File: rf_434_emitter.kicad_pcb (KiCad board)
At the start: 2 copper layers, 133 x 100 mm, 67 parts, among them J1 Conn_Coaxial, J2 Jack-DC, SW1 SW_DIP_x06, SW5 SW_SPDT, SW7 SW_SPDT, SW8 SW_SPDT, U1 HT12E, U2 TLP-434, U3 LM7805_TO220, X1 ENCODER_ANO

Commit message: DIP switch THT
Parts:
- SW2: renamed from SW1; footprint Button_Switch_SMD:SW_DIP_SPSTx06_Slide_6.7x16.8mm_W8.61mm_P2.54mm_LowProfile -> Button_Switch_THT:SW_DIP_SPSTx06_Slide_9.78x17.42mm_W7.62mm_P2.54mm
- moved SW2 7.81 mm to (174.0, 109.3)
- renumbered C4 to C1, C3 to C2, C5 to C3, C6 to C4, C1 to C5, C2 to C6, D14 to D1, D7 to D10, D8 to D11, D9 to D12, D10 to D13, D11 to D14, D12 to D15, D15 to D2, D13 to D3, D1 to D4, D2 to D5, D3 to D6, D4 to D7, D5 to D8, D6 to D9, H4 to H3, H3 to H4, JP5 to JP1, JP6 to JP2, JP1 to JP4, JP4 to JP5, JP2 to JP6, R29 to R1, R21 to R10, R22 to R11, R23 to R12, R24 to R13, R25 to R14, R26 to R15, R5 to R16, R3 to R17, R2 to R18, R1 to R19, R28 to R2, R4 to R20, R14 to R21, R13 to R22, R12 to R23, R11 to R24, R10 to R25, R9 to R26, R27 to R3, R15 to R4, R16 to R5, R17 to R6, R18 to R7, R19 to R8, R20 to R9, SW5 to SW1, SW7 to SW3, SW8 to SW4, U2 to U1, U3 to U2, U1 to U3
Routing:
- net GND: track 14.0 -> 16.2 mm

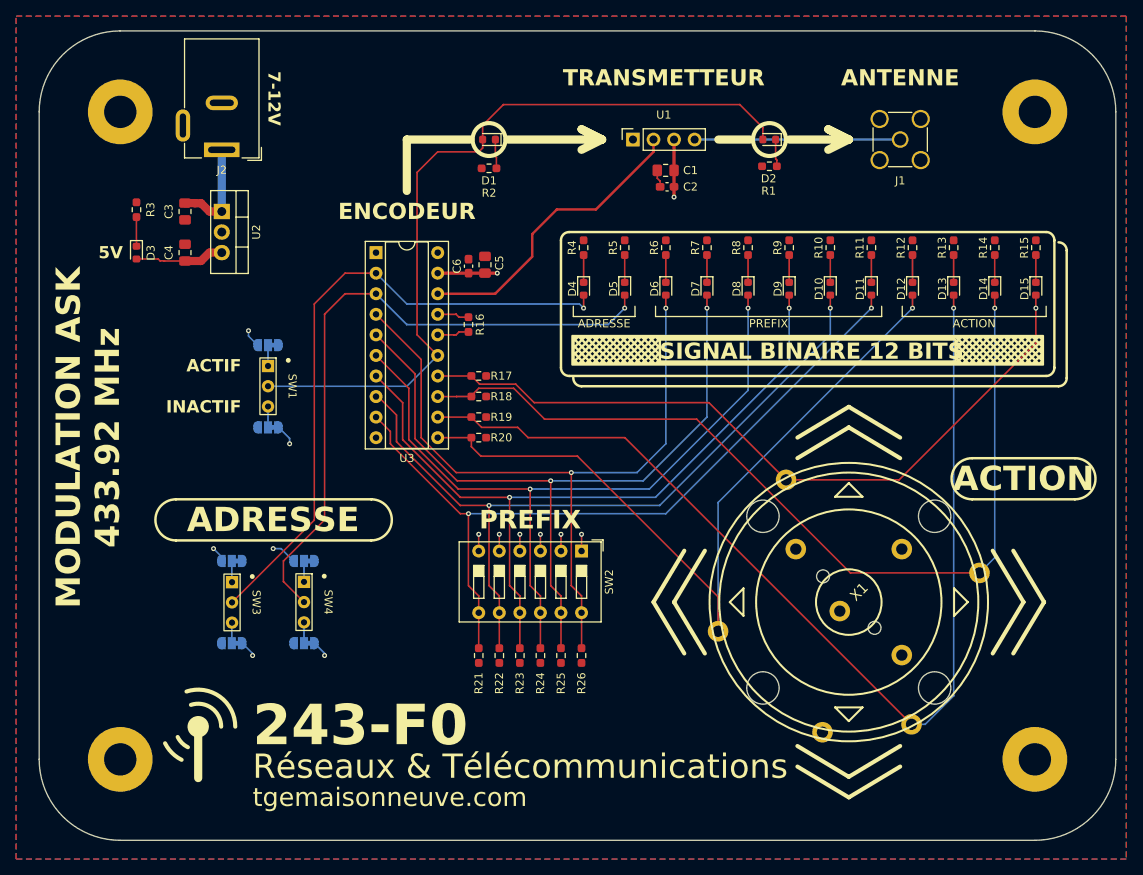
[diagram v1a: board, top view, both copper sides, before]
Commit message: Add D0-D3 connector
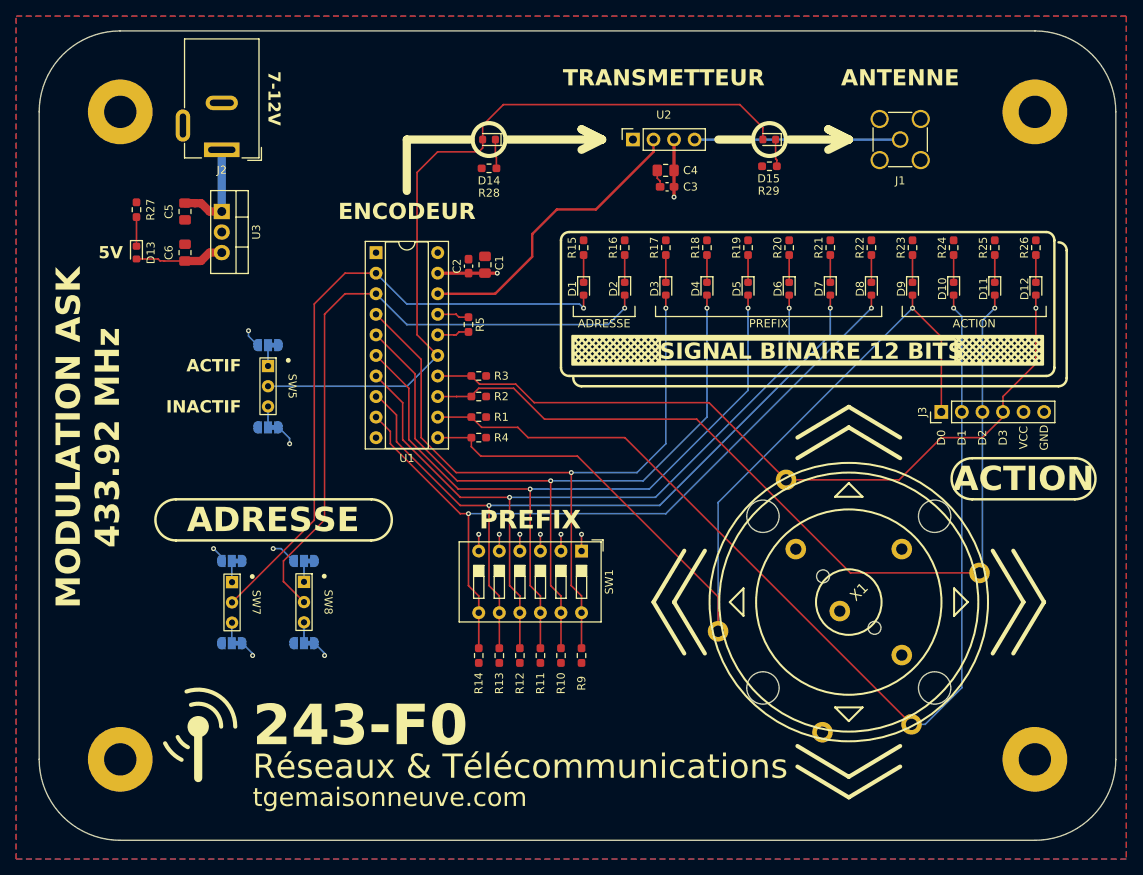
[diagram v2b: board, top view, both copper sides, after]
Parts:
- added J3: Conn_01x06, Connector_PinHeader_2.54mm:PinHeader_1x06_P2.54mm_Vertical, F.Cu at (218.4, 92.1)
- renumbered C5 to C1, C6 to C2, C2 to C3, C1 to C4, C3 to C5, C4 to C6, D4 to D1, D13 to D10, D14 to D11, D15 to D12, D3 to D13, D1 to D14, D2 to D15, D5 to D2, D6 to D3, D7 to D4, D8 to D5, D9 to D6, D10 to D7, D11 to D8, D12 to D9, H4 to H3, H3 to H4, JP4 to JP1, JP6 to JP2, JP5 to JP4, JP1 to JP5, JP2 to JP6, R19 to R1, R25 to R10, R24 to R11, R23 to R12, R22 to R13, R21 to R14, R4 to R15, R5 to R16, R6 to R17, R7 to R18, R8 to R19, R18 to R2, R9 to R20, R10 to R21, R11 to R22, R12 to R23, R13 to R24, R14 to R25, R15 to R26, R3 to R27, R2 to R28, R1 to R29, R17 to R3, R20 to R4, R16 to R5, R26 to R9, SW2 to SW1, SW1 to SW5, SW3 to SW7, SW4 to SW8, U3 to U1, U1 to U2, U2 to U3
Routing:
- net /D0: track 99.2 -> 114.1 mm
- net /D3: track 92.2 -> 95.1 mm
- net /D1: track 130.4 -> 131.3 mm
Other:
- board text added: "D0"
- board text added: "D1"
- board text added: "D2"
- board text added: "D3"

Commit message: Add 3D model Jack connector
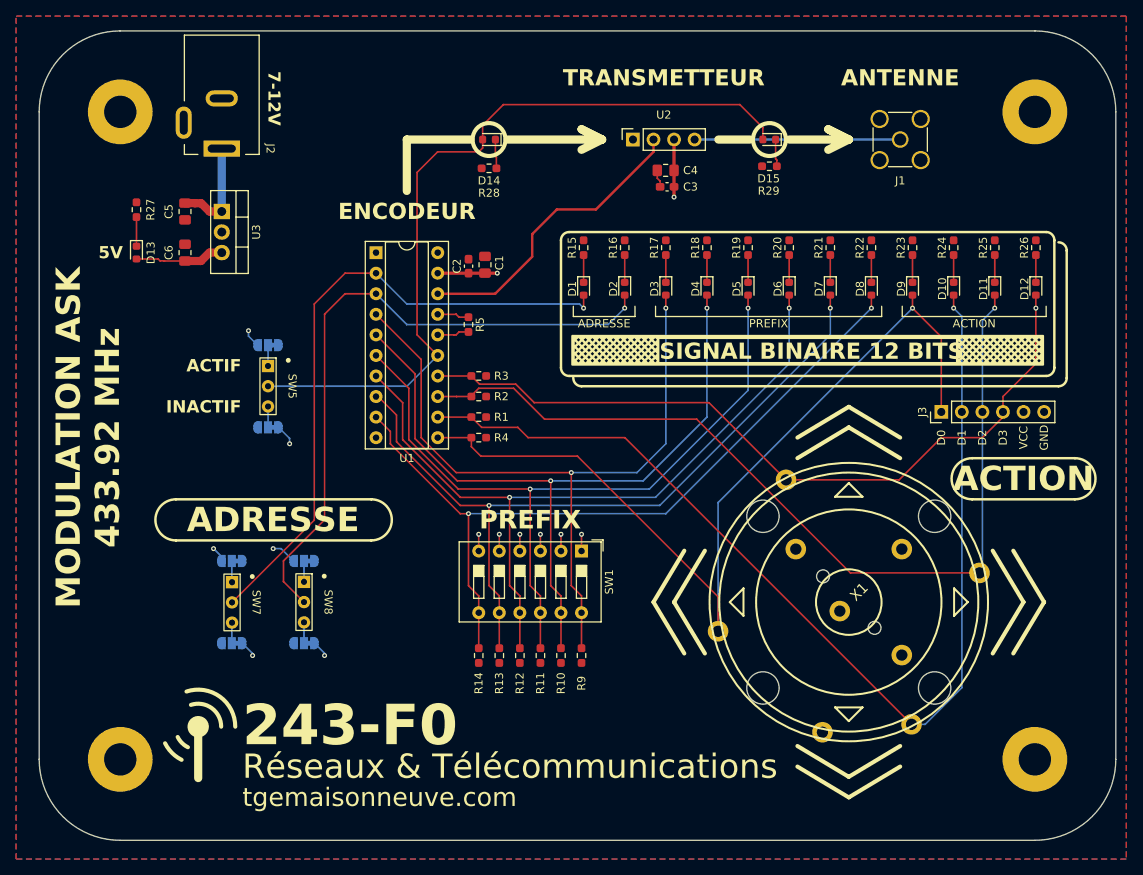
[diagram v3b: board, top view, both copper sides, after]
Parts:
- J2: value Jack-DC -> Barrel_Jack_Switch; footprint Connector_BarrelJack:BarrelJack_Wuerth_6941xx301002 -> Connector_BarrelJack:BarrelJack_Kycon_KLDX-0202-xC_Horizontal
- moved J2 0.15 mm to (129.5, 59.5), turned to -90 degrees
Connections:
- J2 pad 3: (no net) -> unconnected-(J2-Pad3)

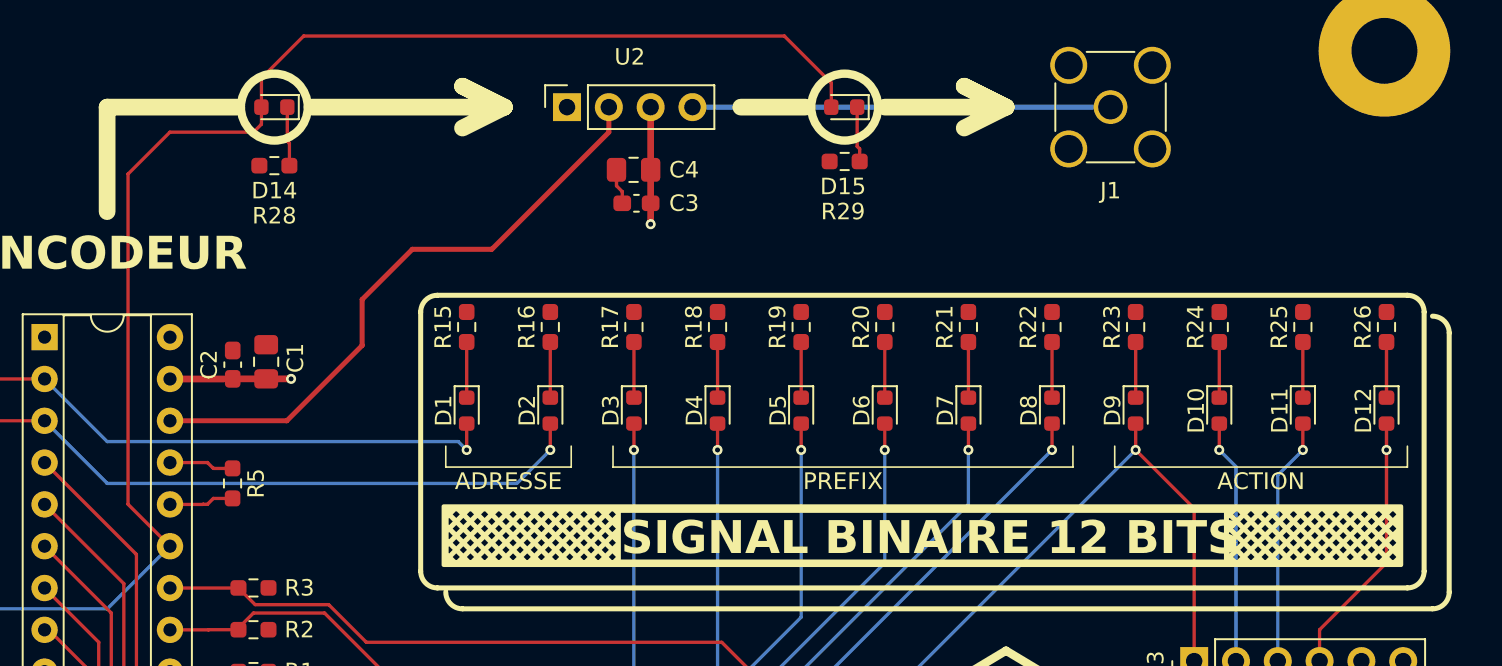
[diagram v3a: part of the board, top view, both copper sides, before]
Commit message: Inversion des LED \TE
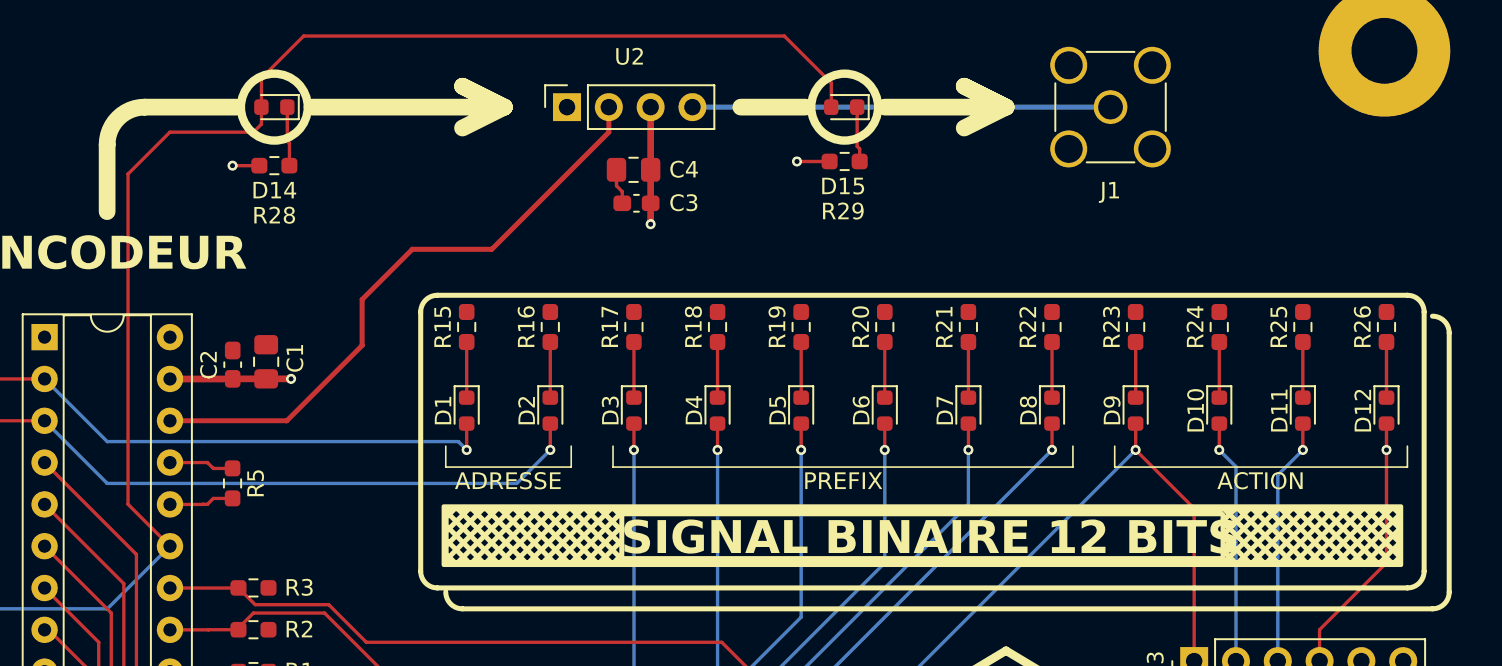
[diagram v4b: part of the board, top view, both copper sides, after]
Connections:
- R28 pad 2: GND -> VCC
- R29 pad 2: GND -> VCC
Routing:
- net VCC: track 39.9 -> 43.6 mm, vias 8 -> 10
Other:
- board text added: "JLCJLCJLC"
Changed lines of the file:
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@@
 			(layers "F.Cu" "F.Paste" "F.Mask")
 			(roundrect_rratio 0.25)
-			(net 1 "GND")
+			(net 2 "VCC")
 			(pintype "passive")
 		)
@@
 			(layers "F.Cu" "F.Paste" "F.Mask")
 			(roundrect_rratio 0.25)
-			(net 1 "GND")
+			(net 2 "VCC")
 			(pintype "passive")
 		)
@@
 				(font
 					(size 1.27 1.27)
+					(thickness 0.15)
 				)
 			)
@@
 				(font
 					(size 1.27 1.27)
+					(thickness 0.15)
 				)
 			)
@@
 				(font
 					(size 1.27 1.27)
+					(thickness 0.15)
 				)
 			)
@@
 	(gr_line
 		(start 152.4 64.77)
-		(end 152.4 58.42)
+		(end 152.4 60.706)
 		(stroke
 			(width 1.016)
@@
 	)
 	(gr_line
-		(start 152.4 58.42)
+		(start 154.686 58.42)
 		(end 160.274 58.42)
 		(stroke
@@
 	)
 	(gr_arc
+		(start 152.4 60.706)
+		(mid 153.069554 59.089554)
+		(end 154.686 58.42)
+		(stroke
+			(width 1.016)
+			(type default)
+		)
+		(layer "F.SilkS")
+	)
+	(gr_arc
 		(start 231.394 69.85)
 		(mid 232.11242 70.14758)
@@
 		)
 	)
+	(gr_text "JLCJLCJLC"
+		(at 224.282 135.128 0)
+		(layer "B.SilkS")
+		(effects
+			(font
+				(size 1.5 1.5)
+				(thickness 0.15)
+			)
+			(justify left mirror)
+		)
+	)
 	(gr_text "GND"
 		(at 131.445 83.82 0)
@@
 	)
 	(segment
+		(start 161.6475 61.975999)
+		(end 160.020001 61.975999)
+		(width 0.2032)
+		(layer "F.Cu")
+		(net 2)
+	)
+	(segment
 		(start 126.9785 73.4275)
 		(end 125 73.4275)
@@
 	)
 	(segment
+		(start 160.020001 61.975999)
+		(end 160.02 61.976)
+		(width 0.2032)
+		(layer "F.Cu")
+		(net 2)
+	)
+	(segment
 		(start 162.062 74.93)
 		(end 160.03 74.93)
@@
 	)
 	(segment
+		(start 196.295 61.722)
+		(end 194.31 61.722)
+		(width 0.2032)
+		(layer "F.Cu")
+		(net 2)
+	)
+	(segment
 		(start 185.42 62.23)
 		(end 185.42 58.42)
@@
 	)
 	(via
+		(at 160.02 61.976)
+		(size 0.6096)
+		(drill 0.3048)
+		(layers "F.Cu" "B.Cu")
+		(net 2)
+	)
+	(via
 		(at 173.99 107.188)
 		(size 0.6096)
@@
 		(size 0.6096)
 		(drill 0.3048)
+		(layers "F.Cu" "B.Cu")
+		(net 2)
+	)
+	(via
+		(at 194.31 61.722)
+		(size 0.6096)
+		(drill 0.3048)

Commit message: ATTENTION
Symbole édité dans le schéma 02 pins à 18 pin
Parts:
- U1: footprint Package_DIP:DIP-20_W7.62mm_Socket -> Package_DIP:DIP-18_W7.62mm_Socket
- moved U1 2.54 mm to (148.6, 74.9)
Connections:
- U1 pad 1: unconnected-(U1-NC-Pad1) -> /A0
- U1 pad 10: GND -> /D0
- U1 pad 11: /D0 -> /D1
- U1 pad 12: /D1 -> /D2
- U1 pad 13: /D2 -> /D3
- U1 pad 14: /D3 -> /~{TE}
- U1 pad 15: /~{TE} -> Net-(U1-OSC2)
- U1 pad 16: Net-(U1-OSC2) -> Net-(U1-OSC1)
- U1 pad 17: Net-(U1-OSC1) -> /DOUT
- U1 pad 18: /DOUT -> VCC
- U1 pad 2: /A0 -> /A1
- U1 pad 3: /A1 -> /A2
- U1 pad 4: /A2 -> /A3
- U1 pad 5: /A3 -> /A4
- U1 pad 6: /A4 -> /A5
- U1 pad 7: /A5 -> /A6
- U1 pad 8: /A6 -> /A7
- U1 pad 9: /A7 -> GND
